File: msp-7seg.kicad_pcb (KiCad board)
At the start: 2 copper layers, 50 x 25 mm, 35 parts, among them P1 CONN_11, P3 I2C, Q1 PNP, Q2 PNP, Q3 PNP, Q4 PNP, U1 MSP430G2553IN20, U2 74HC595, U3 LP2985LV, X1 CRYSTAL

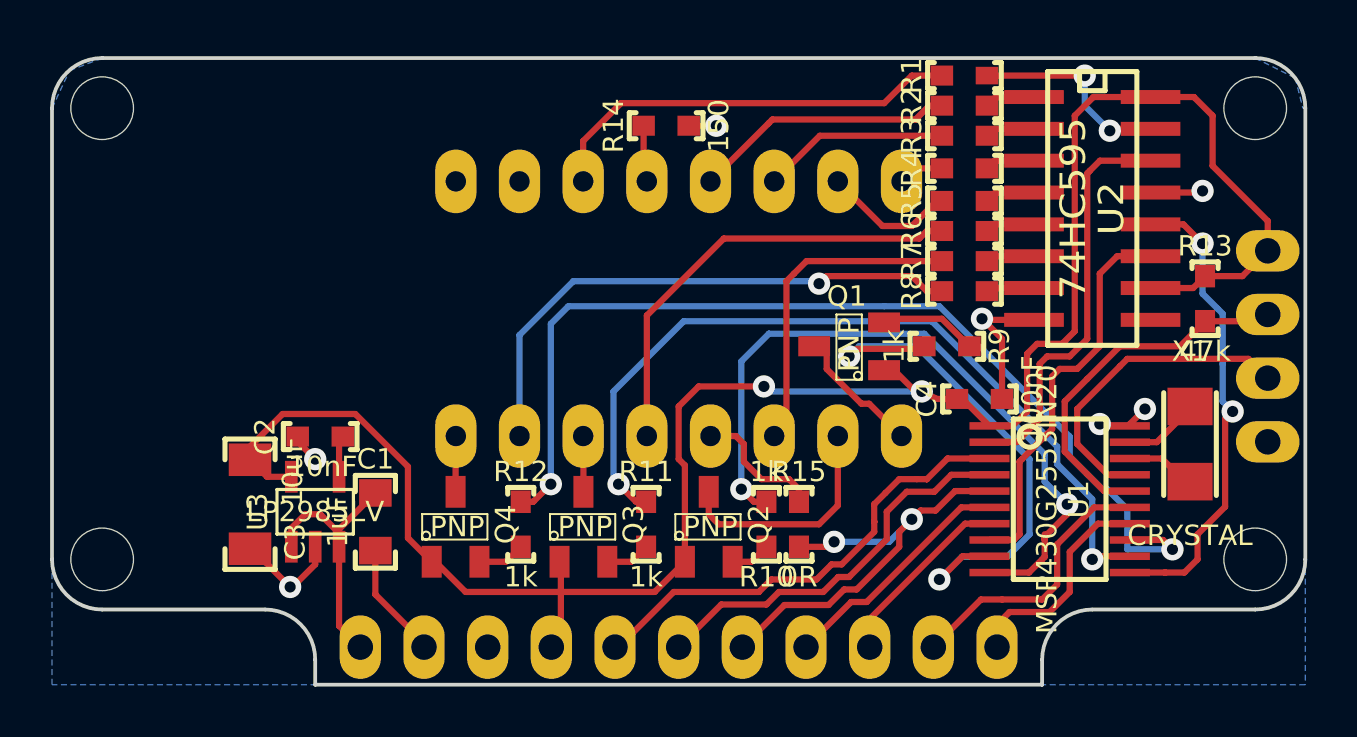
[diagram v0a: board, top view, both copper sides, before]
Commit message: Spread out components and added reset button
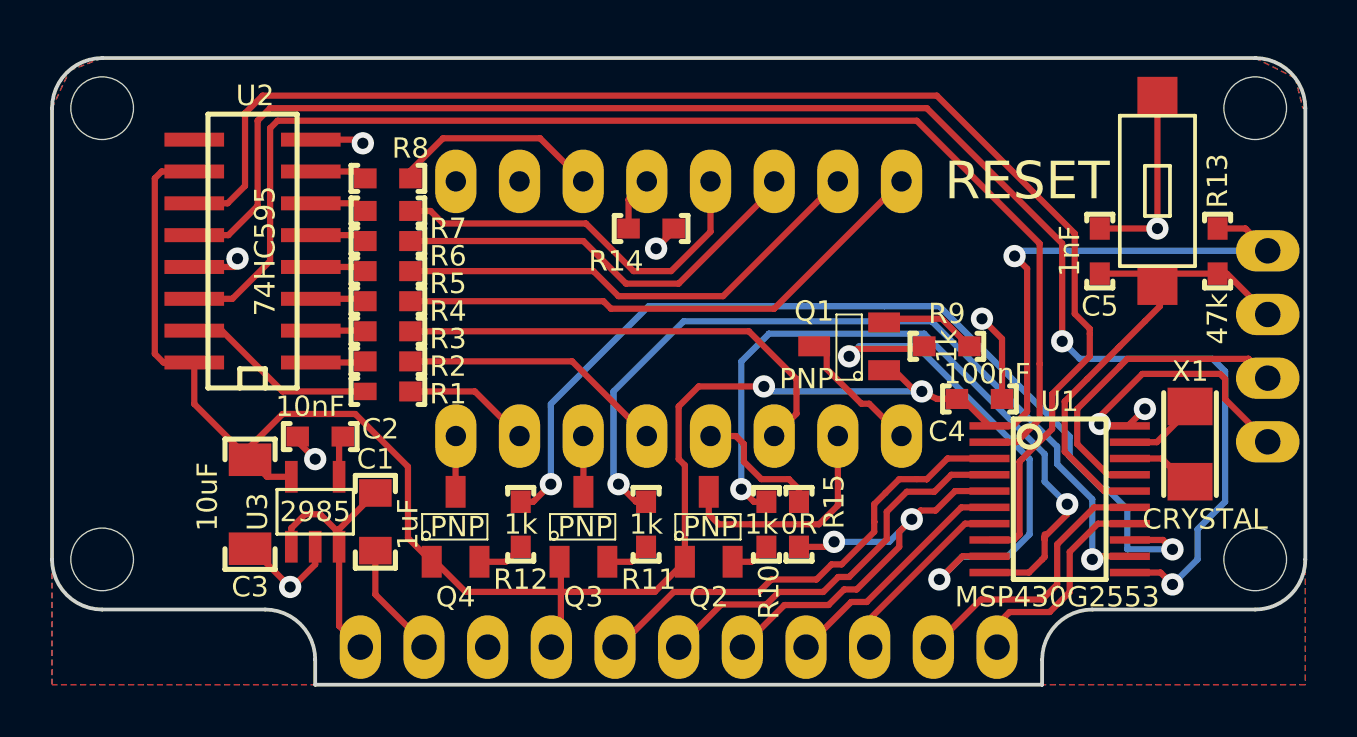
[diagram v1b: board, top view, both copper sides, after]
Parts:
- added C5: 1nF, Custom_SMD:SMD_0603, F.Cu at (141.8, 107.7)
- added SW1: RESET, Custom_SMD:3x6_smd_button, F.Cu at (144.1, 105.3)
- U1: value MSP430G2553IN20 -> MSP430G2553
- U3: value LP2985LV -> 2985
- moved U2 33.5 mm to (108.0, 107.7), turned to 90 degrees
- moved R1 26.2 mm to (113.4, 113.3), turned to 180 degrees
- moved R2 25.2 mm to (113.4, 112.1), turned to 180 degrees
- moved R3 24.3 mm to (113.4, 110.9), turned to 180 degrees
- moved R4 23.6 mm to (113.4, 109.7), turned to 180 degrees
- moved R8 23.4 mm to (113.4, 104.8), turned to 180 degrees
- moved R5 23.2 mm to (113.4, 108.5), turned to 180 degrees
- moved R7 23.1 mm to (113.4, 106.1), turned to 180 degrees
- moved R6 23.0 mm to (113.4, 107.3), turned to 180 degrees
- moved R14 4.14 mm to (123.9, 106.8)
- moved R13 1.96 mm to (146.5, 107.7)
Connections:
- R1 pad 1: /F -> /DP
- R2 pad 1: /C -> /E
- R3 pad 1: /A -> /D
- R6 pad 1: /E -> /A
- R7 pad 1: /D -> /C
- R8 pad 1: /DP -> /F
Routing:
- net /SerialLatch: track 19.0 -> 63.1 mm
- net /SerialClock: track 15.7 -> 55.6 mm
- net /SerialData: track 16.2 -> 51.2 mm
- net /B: track 1.83 -> 21.8 mm
- net /DP: track 22.2 -> 5.09 mm, vias 1 -> 0
- net GND: track 21.1 -> 38.0 mm, vias 7 -> 9
- net /G: track 5.30 -> 19.4 mm
- net /A: track 7.44 -> 17.1 mm
- net /F: track 17.0 -> 8.44 mm
- net /E: track 18.0 -> 10.7 mm
- net /D: track 12.9 -> 18.8 mm
- net /C: track 10.5 -> 15.6 mm
- net /RESET: track 14.8 -> 19.2 mm
- net VCC: track 82.6 -> 85.9 mm, vias 2 -> 3
- net /TEST: track 12.8 -> 14.9 mm
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- added copper zone on F.Cu, net GND
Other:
- board text added: "+"
- board text added: "-"
- board text added: "R"
- board text added: "T"

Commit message: Cleaned up silkscreen, added gerbers, schematic and images
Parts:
- added SYM: Symbol_OSHW-Logo_SilkScreen_07Jul2012, Footprint_Symbols:Symbol_OSHW-Logo_SilkScreen, F.Cu at (120.0, 109.0)
- X1: value CRYSTAL -> 32KHz
- moved SYM 4.62 mm to (108.7, 106.8)
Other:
- board text added: "1.1 Rx"
- board text added: "1.2 Tx"
- board text added: "1.6 SCL"
- board text added: "1.7 SDA"
- board text added: "Copyright © 2014, Niels Kjøller Hansen"
- board text added: "Licensed under CERN OHL v.1.2"
- board text added: "MiniSP 7 segment"
- board text added: "http://lab.kjlr.dk/p/minisp-7seg"
- board text removed: "1.1"
- board text removed: "1.2"
- board text removed: "1.6"
- board text removed: "1.7"

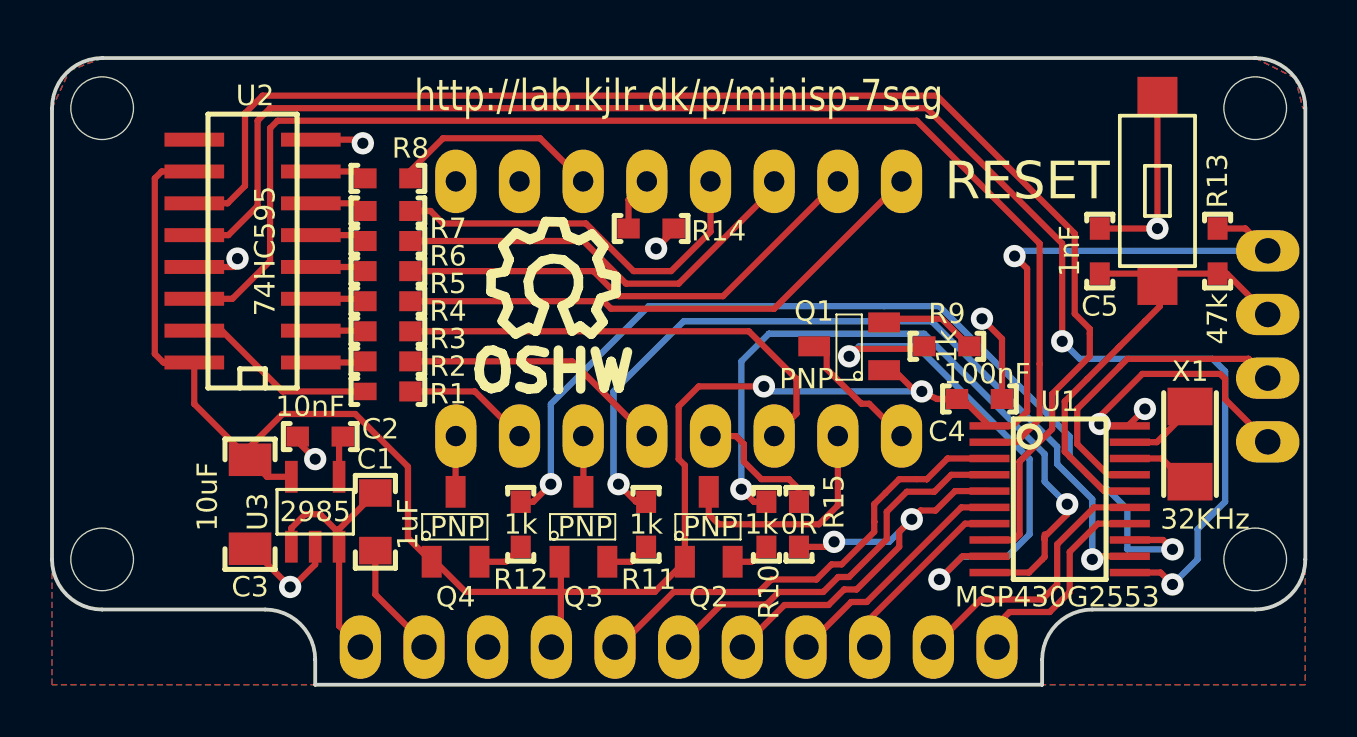
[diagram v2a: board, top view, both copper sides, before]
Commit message: Added breakout for shift register
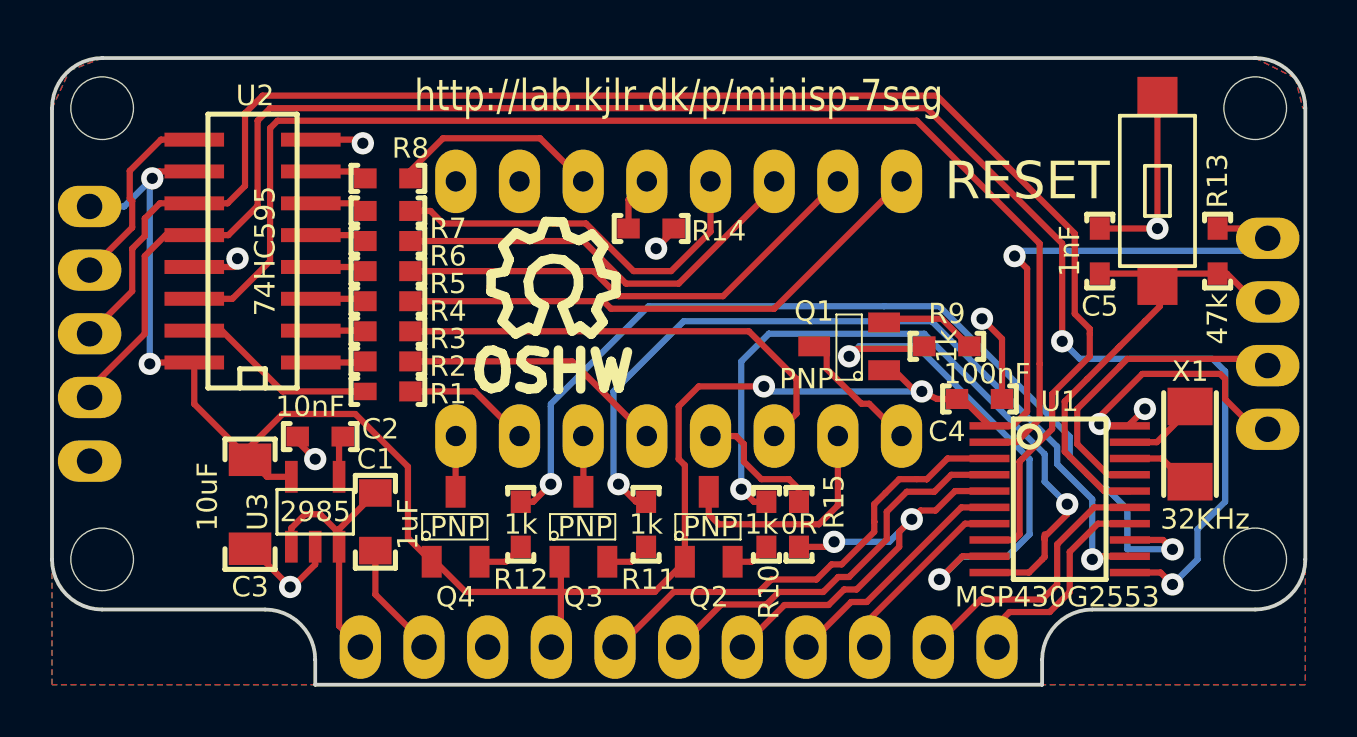
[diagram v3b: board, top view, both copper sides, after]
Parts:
- added P2: Serial, Custom_pinheaders:Pinrow_5p_oval, F.Cu at (101.5, 111.0)
- P1: value CONN_11 -> IO
- moved P3 0.50 mm to (148.5, 111.0)
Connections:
- U2 pad 9: Net-(U2-Pad9) -> /SerialOut
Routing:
- net /SerialLatch: track 63.1 -> 72.0 mm
- net /SerialOut: track 0.00 -> 7.80 mm
- net /SerialClock: track 55.6 -> 63.3 mm
- net VCC: track 85.9 -> 89.6 mm, vias 3 -> 5
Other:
- board text added: "C"
- board text added: "D"
- board text added: "L"
- board text added: "MiniSP 7segment"
- board text added: "SBW"
- board text added: "Shift"
- board text removed: "MiniSP 7 segment"

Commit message: Made a 5x5cm mini panel and added to the README.
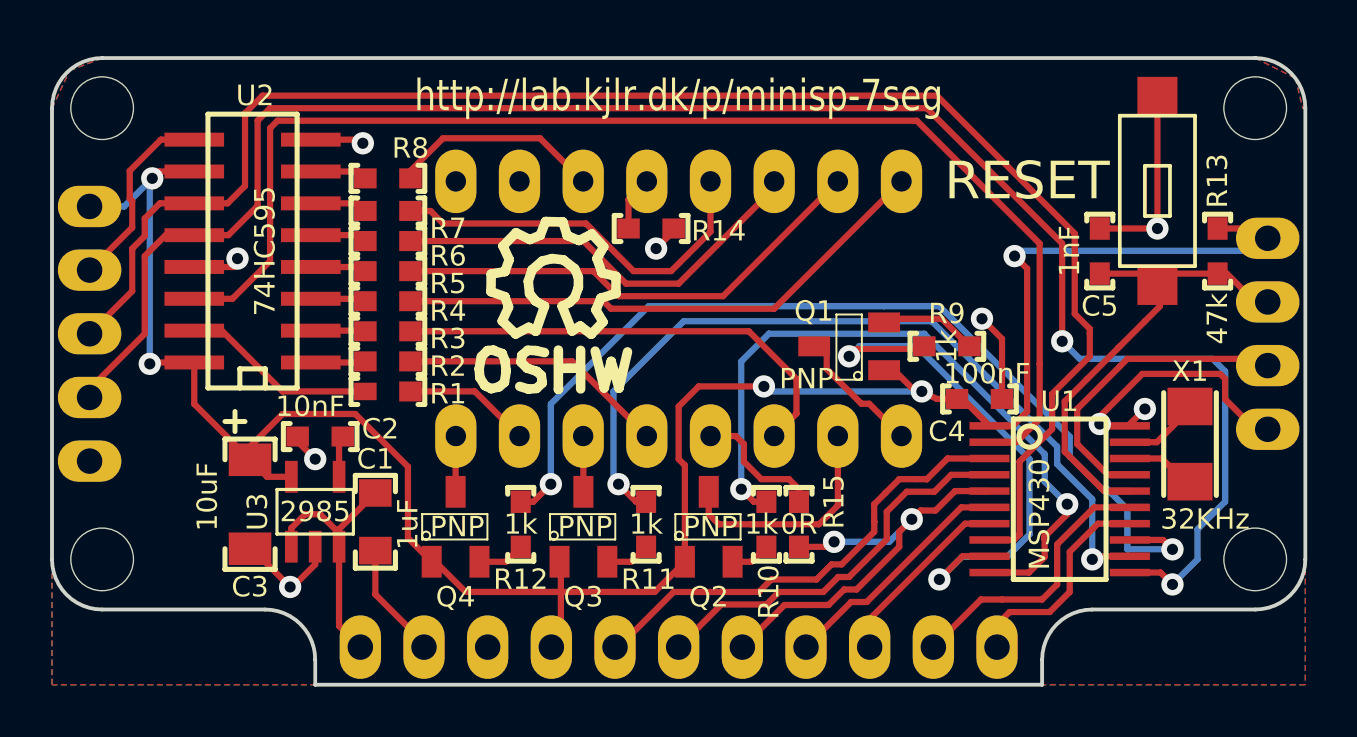
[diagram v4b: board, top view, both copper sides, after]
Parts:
- U1: value MSP430G2553 -> MSP430
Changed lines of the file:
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@@
     (area 76.12123 96.37882 174.07689 127.884708)
     (thickness 1.6)
-    (drawings 42)
+    (drawings 44)
     (tracks 421)
     (zones 0)
@@
     (trace_clearance 0.248)
     (zone_clearance 0.254)
-    (zone_45_only no)
+    (zone_45_only yes)
     (trace_min 0.25)
     (segment_width 0.2)
@@
     (pad_drill 1.016)
     (pad_to_mask_clearance 0)
-    (aux_axis_origin 0 0)
+    (aux_axis_origin 125 125)
+    (grid_origin 100 125)
     (visible_elements FFFFFF7F)
     (pcbplotparams
-      (layerselection 284196865)
+      (layerselection 16285697)
       (usegerberextensions true)
       (excludeedgelayer true)
@@
       (viasonmask false)
       (mode 1)
-      (useauxorigin false)
+      (useauxorigin true)
       (hpglpennumber 1)
       (hpglpenspeed 20)
@@
       (effects (font (size 0.8128 0.8128) (thickness 0.2032)))
     )
-    (fp_text value MSP430G2553 (at 3.9 0.1 360) (layer F.SilkS)
-      (effects (font (size 0.8128 0.8128) (thickness 0.2032)))
+    (fp_text value MSP430 (at 0.6 0.8 270) (layer F.SilkS)
+      (effects (font (size 0.8128 0.8128) (thickness 0.175)))
     )
     (fp_line (start 3.2 1.85) (end -3.2 1.85) (layer F.SilkS) (width 0.2032))
@@
       (net 29 GND))
   )
+  (gr_line (start 106.9 114.5) (end 107.7 114.5) (angle 90) (layer F.SilkS) (width 0.2))
+  (gr_line (start 107.3 114.9) (end 107.3 114.1) (angle 90) (layer F.SilkS) (width 0.2))
   (gr_text Shift (at 101.9 104.4) (layer B.SilkS)
     (effects (font (size 1 1) (thickness 0.2032)) (justify mirror))
@@
     )
   )
-  (zone (net 0) (net_name "") (layer B.Cu) (hatch edge 0.508)
-    (connect_pads (clearance 0.254))
-    (min_thickness 0.254)
-    (keepout (tracks allowed) (vias allowed) (copperpour not_allowed))
-    (fill (arc_segments 16) (thermal_gap 0.381) (thermal_bridge_width 0.3048))
-    (polygon
-      (pts
-        (xy 142.2 114.7) (xy 142.2 116.2) (xy 143.6 116.2) (xy 144.3 116.9) (xy 144.3 117.6)
-        (xy 146.1 117.6) (xy 146.1 113) (xy 143.9 113) (xy 142.4 114.5) (xy 142.2 114.5)
-        (xy 142.2 114.6) (xy 142.1 114.6) (xy 142.1 114.4) (xy 142.4 114.4) (xy 143.9 112.9)
-        (xy 146.1 112.9) (xy 146.2 113) (xy 146.2 117.6) (xy 146.1 117.7) (xy 144.3 117.7)
-        (xy 144.2 117.6) (xy 144.2 116.9) (xy 143.6 116.3) (xy 142.2 116.3) (xy 142.1 116.2)
-        (xy 142.1 114.7)
-      )
-    )
-  )
   (zone (net 29) (net_name GND) (layer F.Cu) (hatch edge 0.508)
     (connect_pads (clearance 0.254))
@@
       )
     )
+  )
+  (zone (net 0) (net_name "") (layer B.Cu) (hatch edge 0.508)
+    (connect_pads (clearance 0.254))
+    (min_thickness 0.254)
+    (keepout (tracks allowed) (vias allowed) (copperpour not_allowed))
+    (fill (arc_segments 16) (thermal_gap 0.381) (thermal_bridge_width 0.3048))
+    (polygon
+      (pts
+        (xy 142.1 116.1) (xy 142.1 114.4) (xy 142.3 114.4) (xy 143.7 113) (xy 143.8 112.9)
+        (xy 146.6 112.9) (xy 146.6 118) (xy 144.2 118) (xy 144.2 116.5) (xy 144 116.3)
+        (xy 142.1 116.3)
+      )
+    )
+    (polygon
+      (pts        (xy 142.2 114.5) (xy 142.3 114.5) (xy 143.8 113) (xy 146.5 113) (xy 146.5 117.9)
+        (xy 144.3 117.9) (xy 144.3 116.5) (xy 144 116.2) (xy 142.2 116.2)
+      )
+    )
+  )
+  (zone (net 0) (net_name "") (layer F.Cu) (hatch edge 0.508)
+    (connect_pads (clearance 0.254))
+    (min_thickness 0.254)
+    (keepout (tracks allowed) (vias allowed) (copperpour not_allowed))
+    (fill (arc_segments 16) (thermal_gap 0.381) (thermal_bridge_width 0.3048))
+    (polygon
+      (pts
+        (xy 142.1 116.1) (xy 142.1 114.4) (xy 142.3 114.4) (xy 143.7 113) (xy 143.8 112.9)
+        (xy 146.6 112.9) (xy 146.6 118) (xy 144.2 118) (xy 144.2 116.5) (xy 144 116.3)
+        (xy 142.1 116.3)
+      )
+    )
